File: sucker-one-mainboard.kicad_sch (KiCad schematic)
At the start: 112 parts, among them J1 JST NC Valve, J10 JST Motor, J11 Conn_02x04_Odd_Even, J2 JST NO Valve, J3 6P4C, J4 JST 3 Way Valve, J5 Jack-DC, J6 Phoenix Contact 1733570, J7 QWIIC I2C, J8 SPI, J9 52271-1079, Q1 BSS138, Q2 BSS138, Q3 BSS138, Q4 STN4NF20L, Q5 FDN304PZ, SW2 RST, U1 LD1117S33TR, U2 LM2596SX-5.0/NOPB, U3 LM358D, U4 STM32F401CDUx, Y1 8MHz(16pf)

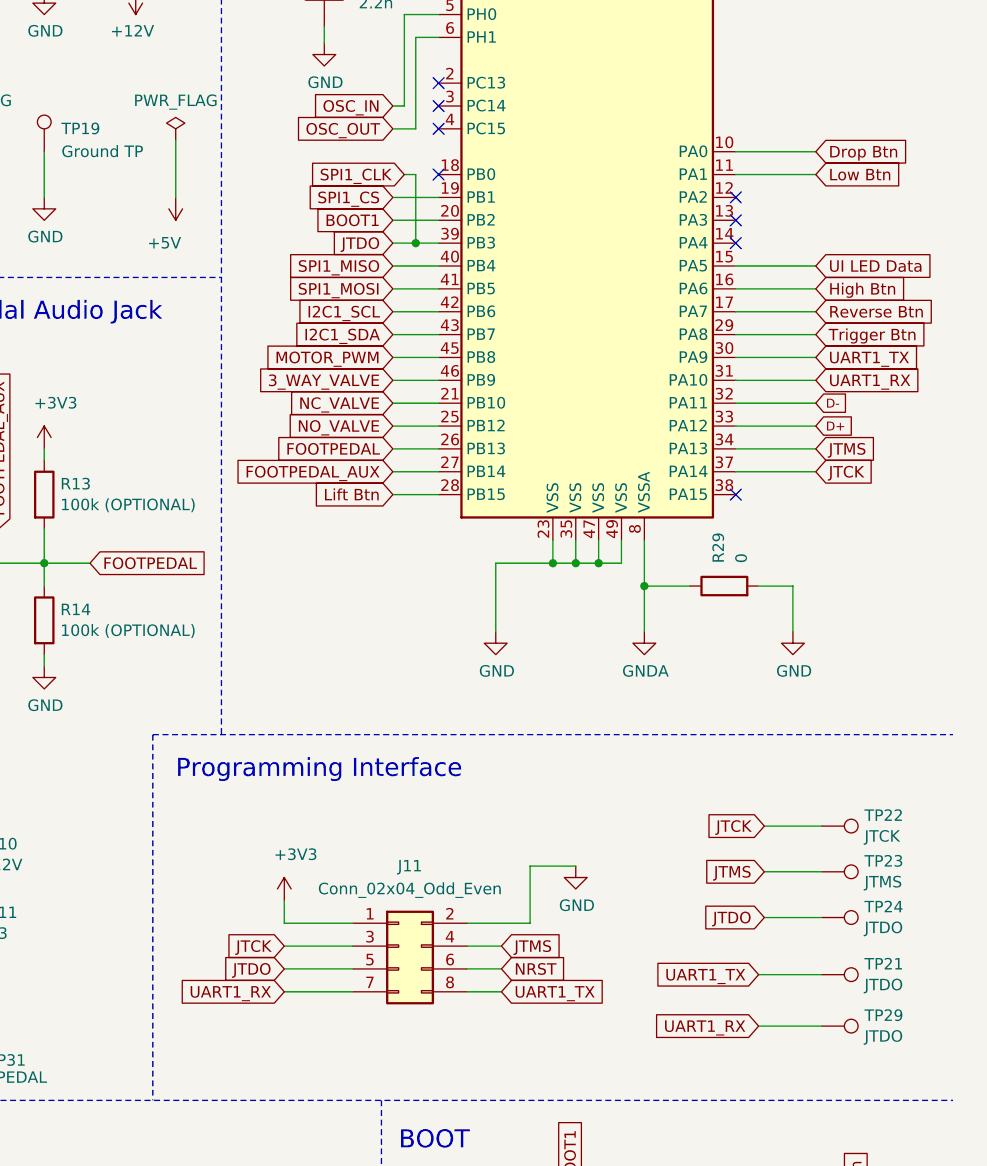
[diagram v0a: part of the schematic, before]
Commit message: finished schematics and assigned footprints
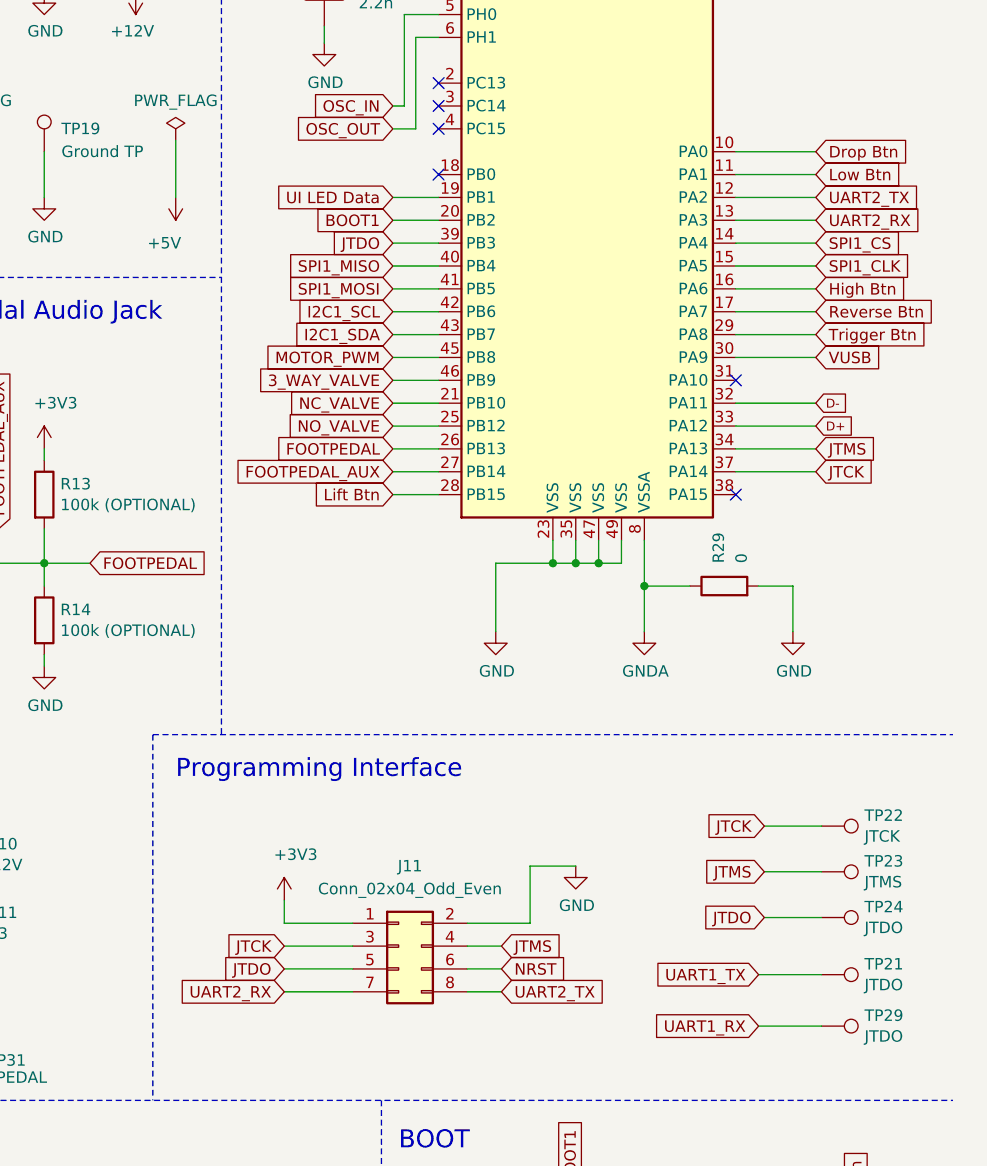
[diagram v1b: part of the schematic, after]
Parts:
- C9: footprint (none) -> Capacitor_SMD:C_0603_1608Metric_Pad1.08x0.95mm_HandSolder
- D1: footprint (none) -> Diode_SMD:D_SMB
- F1: footprint (none) -> Fuse:Fuse_1812_4532Metric_Pad1.30x3.40mm_HandSolder; Source https://lcsc.com/product-detail/Surface-Mount-Fuses_Littelf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 -> https://lcsc.com/product-detail/PTC-Resettable-Fuses_Littel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
- J11: footprint (none) -> Connector_PinHeader_2.00mm:PinHeader_2x04_P2.00mm_Vertical
- J5: footprint (none) -> Connector_BarrelJack:BarrelJack_Wuerth_6941xx301002
- J7: footprint (none) -> Connector_JST:JST_SH_BM04B-SRSS-TB_1x04-1MP_P1.00mm_Vertical
- J8: footprint (none) -> Connector_JST:JST_SH_BM06B-SRSS-TB_1x06-1MP_P1.00mm_Vertical
- J9: footprint Molex-52271-1079-* -> Molex 52271-1079:Molex-52271-1079-Manufacturer_Recommended
- Q5: footprint ON_Semi-FDN304PZ-* -> FDN304PZ:ON_Semi-FDN304PZ-0
- R21, R22, R26, R27, R28, R29: footprint (none) -> Resistor_SMD:R_0603_1608Metric_Pad0.98x0.95mm_HandSolder
- U3: footprint (none) -> LM358D:SOIC127P599X175-8N
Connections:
- net JTDO: no longer J8.3 (Pin_3), TP26.1
- net SPI1_CS: now also U4.14 (PA4); no longer U4.19 (PB1)
- net UART1_RX: no longer J11.7 (Pin_7), U4.31 (PA10)
- net UART1_TX: no longer J11.8 (Pin_8), U4.30 (PA9)
- net UI LED Data: now also U4.19 (PB1); no longer U4.15 (PA5)
- net VUSB: now also U4.30 (PA9)
- net UART2_TX: now reaches U4.12 (PA2)
- net UART2_TX: now also J11.8 (Pin_8)
- net UART2_RX: now reaches U4.13 (PA3)
- net UART2_RX: now also J11.7 (Pin_7)
- new net SPI1_CLK: J8.3 (Pin_3), TP26.1, U4.15 (PA5)
- no-connect marks 12 -> 10

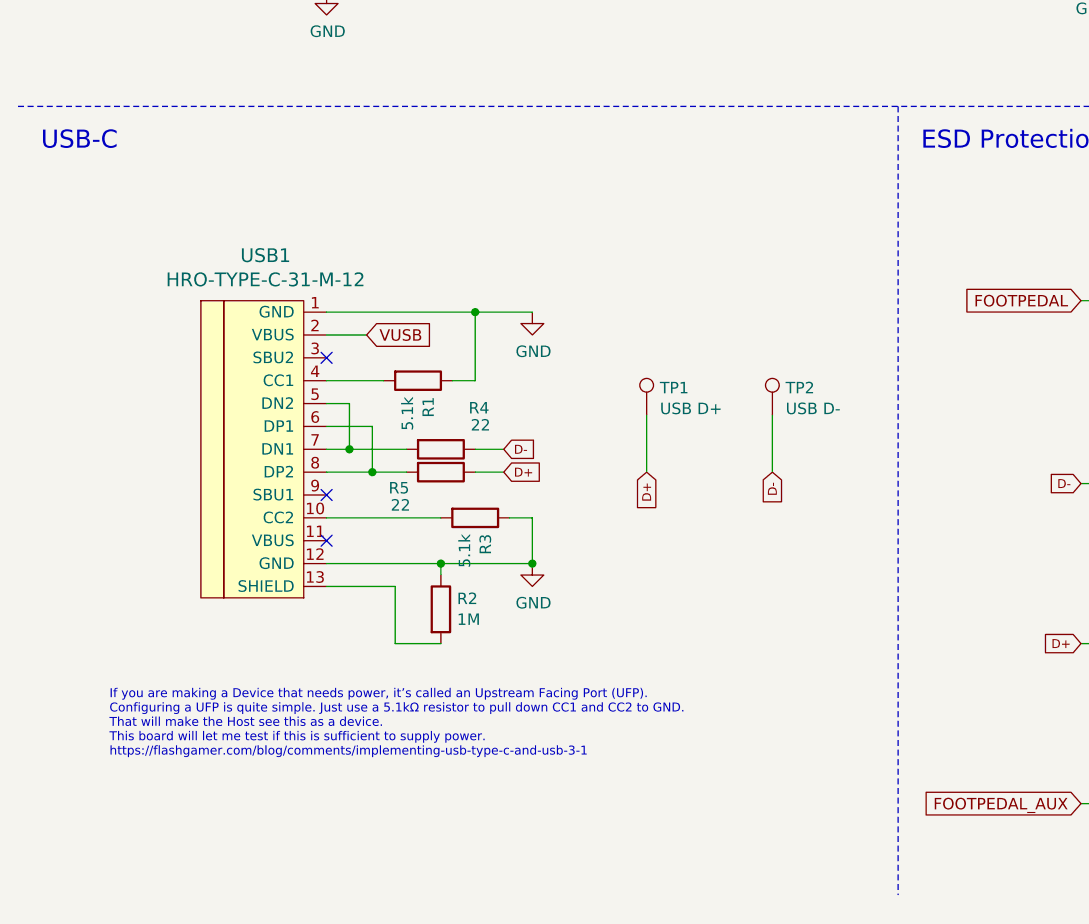
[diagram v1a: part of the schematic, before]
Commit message: Update USB-C
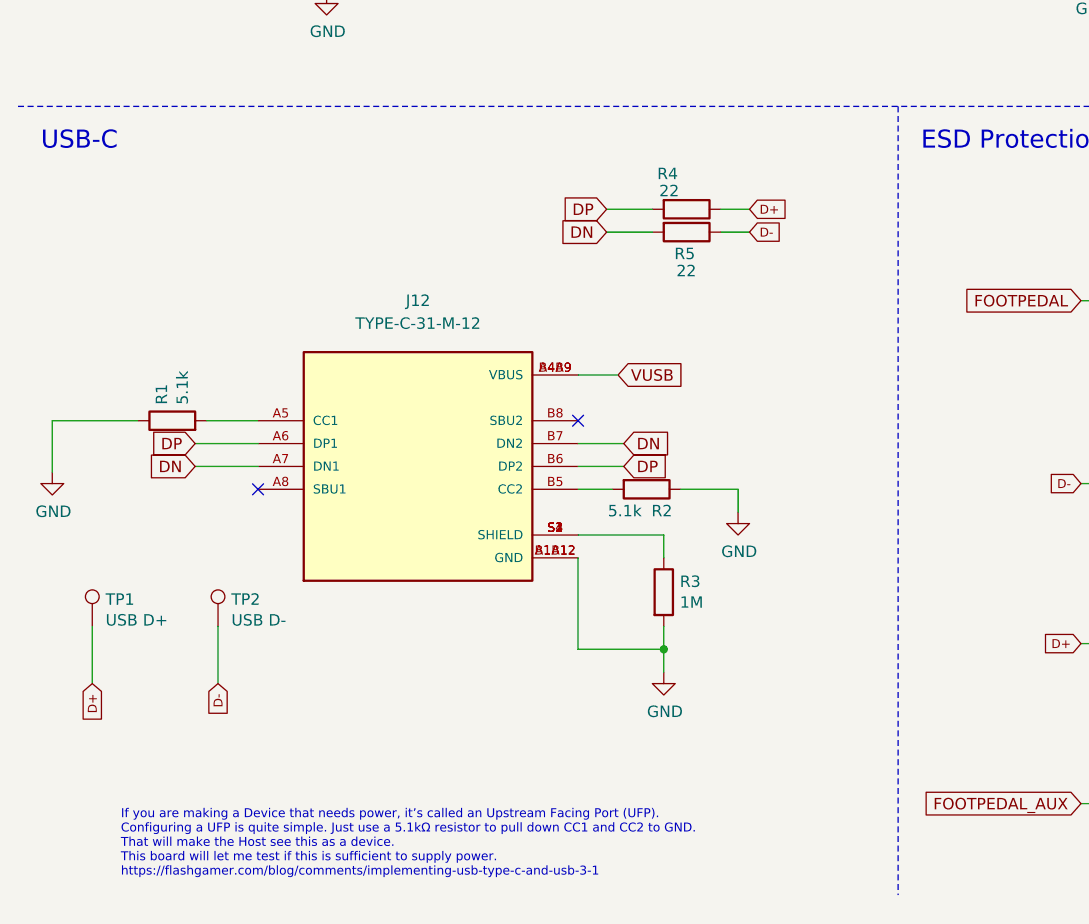
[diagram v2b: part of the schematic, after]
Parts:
- removed USB1: HRO-TYPE-C-31-M-12, sucker-one-mainboard:HRO-TYPE-C-31-M-12, symbol sucker-one-mainboard-rescue:HRO-TYPE-C-31-M-12-Type-C
- added J12: TYPE-C-31-M-12, HRO_TYPE-C-31-M-12, symbol TYPE-C-31-M-12:TYPE-C-31-M-12
- R2: value 1M -> 5.1k
- R3: value 5.1k -> 1M
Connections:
- net D+: now also R4.1; no longer R5.1
- net D-: now also R5.1; no longer R4.1
- net GND: now also R3.2, J12.A1B12 (GND), J12.B1A12 (GND); no longer R3.1
- net VUSB: now also J12.A4B9 (VBUS), J12.B4A9 (VBUS)
- net at R1.2: now also J12.A5 (CC1)
- net at R2.2: now also J12.B5 (CC2)
- net DP: now reaches R4.2
- net DP: now also J12.A6 (DP1), J12.B6 (DP2)
- net DN: now reaches R5.2
- net DN: now also J12.A7 (DN1), J12.B7 (DN2)
- new net: J12.S1 (SHIELD), J12.S2 (SHIELD), J12.S3 (SHIELD), J12.S4 (SHIELD), R3.1
- no-connect marks 10 -> 9
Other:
- moved on the sheet: TP1, TP2

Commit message: Placed components
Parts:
- added SW1: BOOT0, Button_Switch_SMD:SW_SPST_B3U-1000P, symbol Switch:SW_Push
- J12: footprint HRO_TYPE-C-31-M-12 -> TYPE-C-31-M-12:HRO_TYPE-C-31-M-12
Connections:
- net +3V3: now also SW1.1
- net BOOT0: now also SW1.2
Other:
- moved on the sheet: R18, R26, R27, R28, TP20, TP30

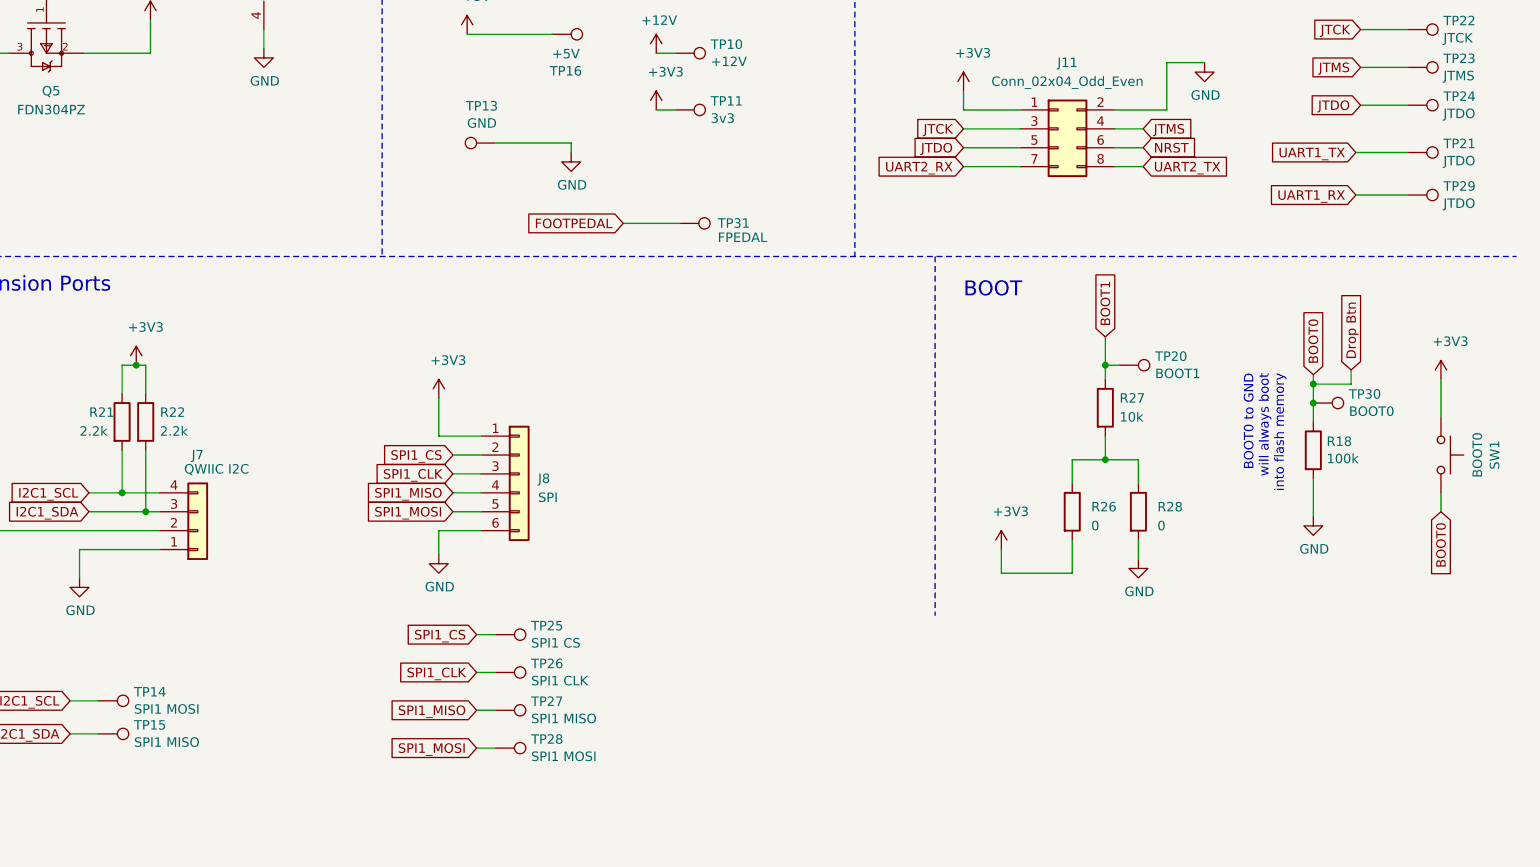
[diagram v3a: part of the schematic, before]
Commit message: pcb layout finished
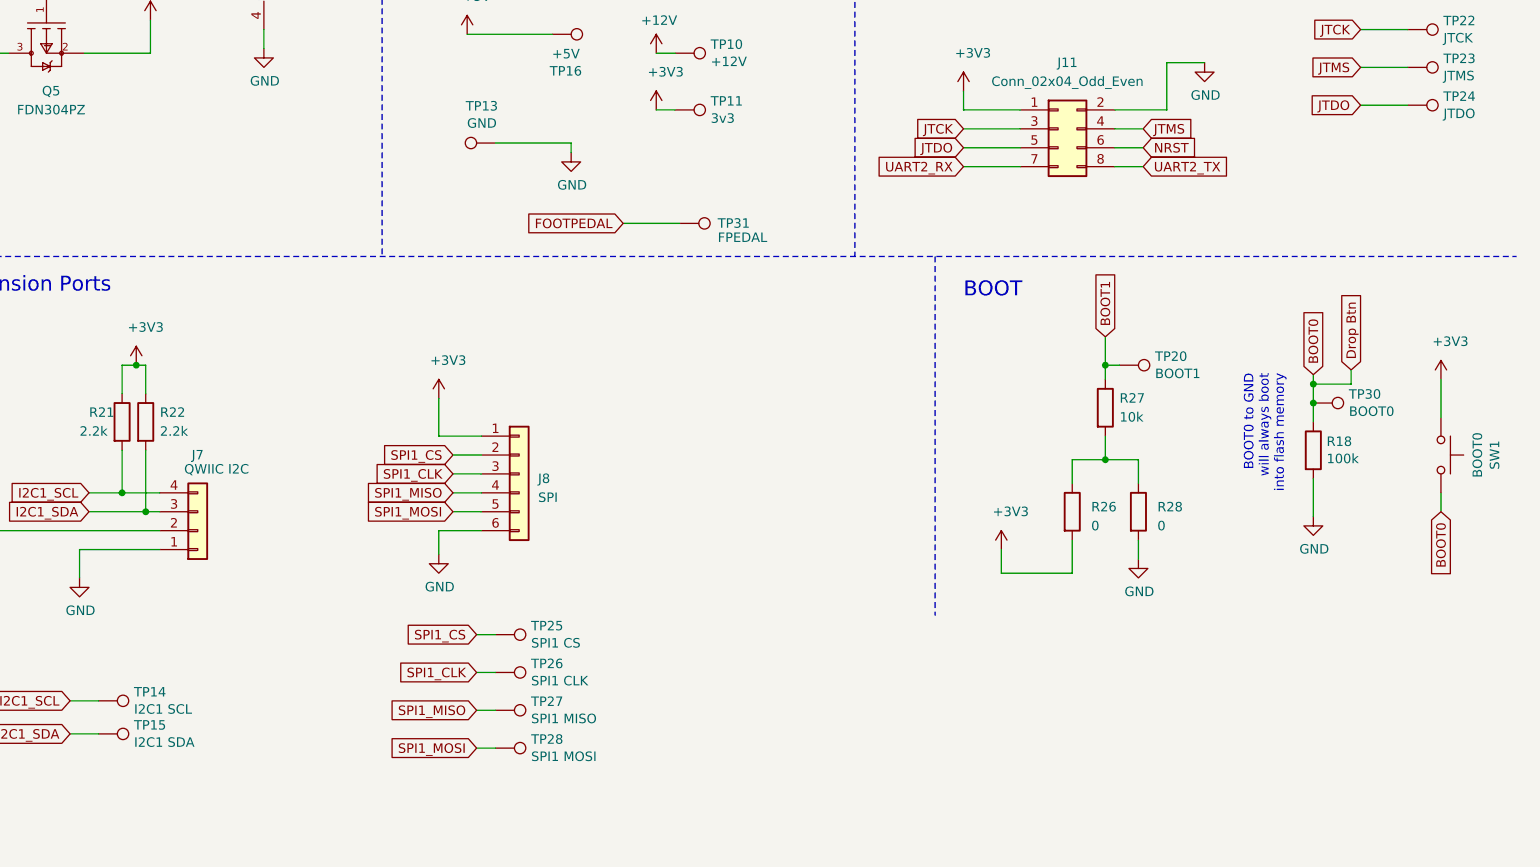
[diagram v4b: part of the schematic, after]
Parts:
- removed TP21, TP29: JTDO, TestPoint:TestPoint_Pad_D2.0mm, symbol Connector:TestPoint
- TP14: value SPI1 MOSI -> I2C1 SCL
- TP15: value SPI1 MISO -> I2C1 SDA
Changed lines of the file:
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@@
     (stroke (width 0) (type solid) (color 0 0 0 0))
   )
-  (wire (pts (xy 384.81 190.5) (xy 391.795 190.5))
-    (stroke (width 0) (type solid) (color 0 0 0 0))
-  )
-  (wire (pts (xy 384.81 196.215) (xy 391.795 196.215))
-    (stroke (width 0) (type solid) (color 0 0 0 0))
-  )
   (wire (pts (xy 385.445 173.99) (xy 391.795 173.99))
     (stroke (width 0) (type solid) (color 0 0 0 0))
@@
     )
   )
-  (global_label "UART1_TX" (shape input) (at 384.81 190.5 180)
-    (effects (font (size 1.27 1.27)) (justify right))
-    (property "Intersheet References" "${INTERSHEET_REFS}" (id 0) (at 769.62 257.81 0)
-      (effects (font (size 1.27 1.27)) hide)
-    )
-  )
-  (global_label "UART1_RX" (shape input) (at 384.81 196.215 180)
-    (effects (font (size 1.27 1.27)) (justify right))
-    (property "Intersheet References" "${INTERSHEET_REFS}" (id 0) (at 769.62 266.065 0)
-      (effects (font (size 1.27 1.27)) hide)
-    )
-  )
   (global_label "JTCK" (shape input) (at 385.445 173.99 180)
     (effects (font (size 1.27 1.27)) (justify right))
@@
       (effects (font (size 1.27 1.27)) (justify left))
     )
-    (property "Value" "SPI1 MOSI" (id 1) (at 220.6752 265.303 90)
+    (property "Value" "I2C1 SCL" (id 1) (at 220.675 265.303 90)
       (effects (font (size 1.27 1.27)) (justify left))
     )
@@
       (effects (font (size 1.27 1.27)) (justify left))
     )
-    (property "Value" "SPI1 MISO" (id 1) (at 220.6752 269.748 90)
+    (property "Value" "I2C1 SDA" (id 1) (at 220.675 269.748 90)
       (effects (font (size 1.27 1.27)) (justify left))
     )
@@
     (pin "1")
   )
-  (symbol (lib_id "Connector:TestPoint") (at 391.795 190.5 270) (unit 1)
-    (in_bom yes) (on_board yes)
-    (property "Reference" "TP21" (id 0) (at 396.5702 189.3316 90)
-      (effects (font (size 1.27 1.27)) (justify left))
-    )
-    (property "Value" "JTDO" (id 1) (at 396.5702 191.643 90)
-      (effects (font (size 1.27 1.27)) (justify left))
-    )
-    (property "Footprint" "TestPoint:TestPoint_Pad_D2.0mm" (id 2) (at 391.795 195.58 0)
-      (effects (font (size 1.27 1.27)) hide)
-    )
-    (property "Datasheet" "~" (id 3) (at 391.795 195.58 0)
-      (effects (font (size 1.27 1.27)) hide)
-    )
-    (pin "1")
-  )
-  (symbol (lib_id "Connector:TestPoint") (at 391.795 196.215 270) (unit 1)
-    (in_bom yes) (on_board yes)
-    (property "Reference" "TP29" (id 0) (at 396.5702 195.0466 90)
-      (effects (font (size 1.27 1.27)) (justify left))
-    )
-    (property "Value" "JTDO" (id 1) (at 396.5702 197.358 90)
-      (effects (font (size 1.27 1.27)) (justify left))
-    )
-    (property "Footprint" "TestPoint:TestPoint_Pad_D2.0mm" (id 2) (at 391.795 201.295 0)
-      (effects (font (size 1.27 1.27)) hide)
-    )
-    (property "Datasheet" "~" (id 3) (at 391.795 201.295 0)
-      (effects (font (size 1.27 1.27)) hide)
-    )
-    (pin "1")
-  )
   (symbol (lib_id "power:+3V3") (at 16.51 22.86 0) (unit 1)
     (in_bom yes) (on_board yes)
@@
     )
     (path "/4e17d8b8-5f32-4f73-87f5-136242d18197"
-      (reference "TP14") (unit 1) (value "SPI1 MOSI") (footprint "TestPoint:TestPoint_Pad_D2.0mm")
+      (reference "TP14") (unit 1) (value "I2C1 SCL") (footprint "TestPoint:TestPoint_Pad_D2.0mm")
     )
     (path "/e8dc0734-a27d-41a5-8543-5657dcdfca22"
-      (reference "TP15") (unit 1) (value "SPI1 MISO") (footprint "TestPoint:TestPoint_Pad_D2.0mm")
+      (reference "TP15") (unit 1) (value "I2C1 SDA") (footprint "TestPoint:TestPoint_Pad_D2.0mm")
     )
     (path "/0c4959e0-1781-4a4d-9818-497489d28469"
@@
       (reference "TP20") (unit 1) (value "BOOT1") (footprint "TestPoint:TestPoint_Pad_D2.0mm")
     )
-    (path "/328a29c3-d9f5-4f6f-974a-057b3145eadb"
-      (reference "TP21") (unit 1) (value "JTDO") (footprint "TestPoint:TestPoint_Pad_D2.0mm")
-    )
     (path "/00000000-0000-0000-0000-00006183370a"
       (reference "TP22") (unit 1) (value "JTCK") (footprint "TestPoint:TestPoint_Pad_D2.0mm")
@@
       (reference "TP28") (unit 1) (value "SPI1 MOSI") (footprint "TestPoint:TestPoint_Pad_D2.0mm")
     )
-    (path "/28d34c62-0a40-43dc-b4be-5e763ee0abfc"
-      (reference "TP29") (unit 1) (value "JTDO") (footprint "TestPoint:TestPoint_Pad_D2.0mm")
-    )
     (path "/00000000-0000-0000-0000-00006164f305"

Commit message: Create schematic PDF
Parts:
- R26: value 0 -> 0 (OPTIONAL)
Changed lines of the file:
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@@
   (symbol (lib_id "Device:R") (at 346.71 238.76 0) (unit 1)
     (in_bom yes) (on_board yes)
-    (property "Reference" "R26" (id 0) (at 349.25 238.125 0)
-      (effects (font (size 1.27 1.27)) (justify left))
-    )
-    (property "Value" "0" (id 1) (at 349.25 240.665 0)
+    (property "Reference" "R26" (id 0) (at 345.44 235.585 90)
+      (effects (font (size 1.27 1.27)) (justify left))
+    )
+    (property "Value" "0 (OPTIONAL)" (id 1) (at 342.9 235.585 90)
       (effects (font (size 1.27 1.27)) (justify left))
     )
@@
     )
     (path "/31053262-e0b1-4d27-a7f3-d007d43e02ce"
-      (reference "R26") (unit 1) (value "0") (footprint "Resistor_SMD:R_0603_1608Metric_Pad0.98x0.95mm_HandSolder")
+      (reference "R26") (unit 1) (value "0 (OPTIONAL)") (footprint "Resistor_SMD:R_0603_1608Metric_Pad0.98x0.95mm_HandSolder")
     )
     (path "/9f1ee356-8fc0-4534-9c27-f6b9984a61de"
